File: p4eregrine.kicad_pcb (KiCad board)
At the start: 6 copper layers, 39.5 x 39.5 mm, 357 parts, among them J5 Conn_Coaxial, Q10 NMOS, Q11 NMOS, Q12 NMOS, Q13 NMOS, Q14 NMOS, Q15 NMOS, Q16 NMOS, Q17 NMOS, Q18 NMOS, Q19 NMOS, Q20 NMOS, Q21 NMOS, Q22 NMOS, Q23 NMOS, Q24 NMOS, Q25 NMOS, Q26 NMOS, Q27 NMOS, Q28 NMOS, Q5 NMOS, Q6 NMOS, Q7 NMOS, Q8 NMOS, Q9 NMOS, U10 FPC-1.0FX-15PWCR-H20, U11 VL53L1CXV0FY1, U12 LIS2MDL, U13 LSM6DS3, U14 PMW3901MB-TXQT_C43496881, U15 TPD2EUSB30A, U16 DRV8328ARUYR, U17 TPS62933, U19 DRV8328ARUYR, U2 LPS22HB, U20 STM32G071GBU6, U22 DRV8328ARUYR, U23 STM32G071GBU6, U25 DRV8328ARUYR, U26 STM32G071GBU6, U3 W25Q128JVP, U30 STM32G071GBU6, U4 ESP32-C5HF4, U5 LFD182G45DCHD277, U6 TLV62569DBV, U7 GT-USB-7079C, U8 INA190A2IDCKR, U9 TPS2121RUXR, Y1 Crystal_GND24, Y2 Crystal_GND24

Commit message: Update a couple capacitor footprints
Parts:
- C77, C78: footprint Capacitor_SMD:C_0805_2012Metric -> Capacitor_SMD:C_0603_1608Metric
- R49, R51, R6, R7: footprint Capacitor_SMD:C_0201_0603Metric -> Resistor_SMD:R_0201_0603Metric
- U1: value ~ -> ESP32-P4NRW32X
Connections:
- net /MCU/VDD_PSRAM renamed Net-(U1-VDDO_PSRAM)
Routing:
- net GND: track 237.9 -> 238.8 mm

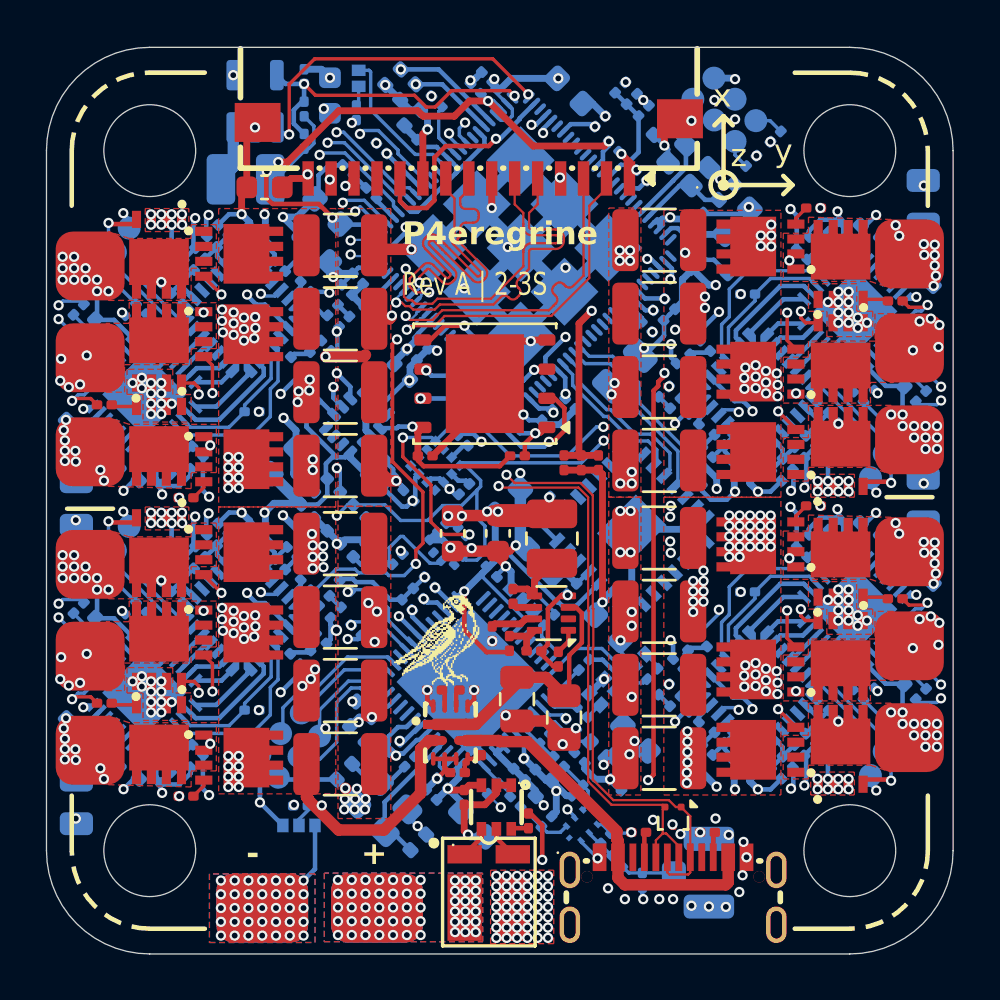
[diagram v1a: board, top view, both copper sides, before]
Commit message: Fix stackup settings in kicad
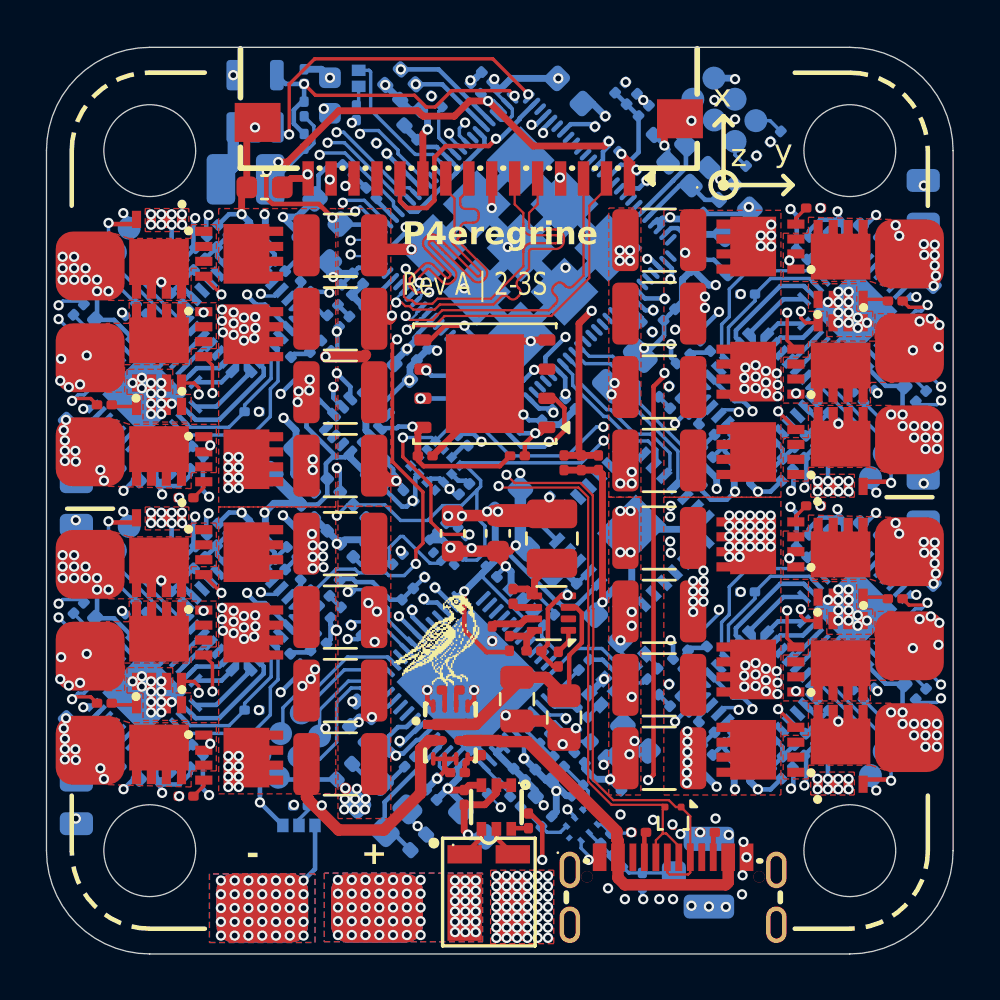
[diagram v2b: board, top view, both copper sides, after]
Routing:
- net GND: track 238.8 -> 238.7 mm, vias 242 -> 243
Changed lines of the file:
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@@
 	(generator_version "10.0")
 	(general
-		(thickness 1.607428)
+		(thickness 1.166)
 		(legacy_teardrops no)
 	)
 	(paper "A4")
 	(layers
-		(0 "F.Cu" signal)
+		(0 "F.Cu" mixed)
 		(4 "In1.Cu" power "F.GND")
 		(6 "In2.Cu" mixed "InF.Cu")
 		(8 "In3.Cu" mixed "InB.Cu")
 		(10 "In4.Cu" power "B.GND")
-		(2 "B.Cu" signal)
+		(2 "B.Cu" mixed)
 		(9 "F.Adhes" user "F.Adhesive")
 		(11 "B.Adhes" user "B.Adhesive")
@@
 		(31 "F.CrtYd" user "F.Courtyard")
 		(29 "B.CrtYd" user "B.Courtyard")
-		(35 "F.Fab" user)
-		(33 "B.Fab" user)
-		(39 "User.1" user)
-		(41 "User.2" user)
-		(43 "User.3" user)
-		(45 "User.4" user)
 	)
 	(setup
@@
 			(layer "dielectric 1"
 				(type "prepreg")
-				(thickness 0.1)
+				(thickness 0.0994)
 				(material "FR4")
 				(epsilon_r 4.1)
@@
 			(layer "dielectric 2"
 				(type "core")
-				(thickness 0.578314)
+				(thickness 0.35)
 				(material "FR4")
 				(epsilon_r 4.6)
@@
 			(layer "dielectric 3"
 				(type "prepreg")
-				(thickness 0.1)
+				(thickness 0.1164)
 				(material "FR4")
 				(epsilon_r 4.1)
@@
 			(layer "dielectric 4"
 				(type "core")
-				(thickness 0.578314)
+				(thickness 0.35)
 				(material "FR4")
 				(epsilon_r 4.6)
@@
 			(layer "dielectric 5"
 				(type "prepreg")
-				(thickness 0.1)
+				(thickness 0.0994)
 				(material "FR4")
 				(epsilon_r 4.1)
@@
 			)
 			(copper_finish "ENIG")
-			(dielectric_constraints no)
+			(dielectric_constraints yes)
 		)
 		(pad_to_mask_clearance 0)
@@
 		(capping no)
 		(filling no)
+		(zone_defaults)
 		(pcbplotparams
 			(layerselection 0x00000000_00000000_55555555_5755f5ff)
@@
 	)
 	(via
-		(at 154.308578 105.428588)
+		(at 153.916729 105.497599)
 		(size 0.45)
 		(drill 0.25)
@@
 	)
 	(via
-		(at 160.482955 106.896387)
+		(at 160.6 107)
 		(size 0.45)
 		(drill 0.25)
@@
 	)
 	(via
+		(at 155.307116 103.523366)
+		(size 0.45)
+		(drill 0.25)
+		(layers "F.Cu" "B.Cu")
+		(remove_unused_layers yes)
+		(keep_end_layers yes)
+		(zone_layer_connections "In1.Cu" "In4.Cu")
+		(net "GND")
+	)
+	(via
 		(at 165.243759 101.971387)
 		(size 0.45)
@@
 	)
 	(segment
+		(start 153.916729 105.497599)
+		(end 153.916729 105.316729)
+		(width 0.15)
+		(layer "B.Cu")
+		(net "GND")
+	)
+	(segment
 		(start 158.75553 101.56816)
 		(end 159.493759 102.306389)
@@
 	)
 	(segment
+		(start 153.590438 104.990438)
+		(end 153.590438 104.661891)
+		(width 0.15)
+		(layer "B.Cu")
+		(net "GND")
+	)
+	(segment
 		(start 155.301278 94.349078)
 		(end 155.301278 95.929463)
@@
 	)
 	(segment
+		(start 153.916729 105.316729)
+		(end 153.590438 104.990438)
+		(width 0.15)
+		(layer "B.Cu")
+		(net "GND")
+	)
+	(segment
 		(start 147.983081 101.105144)
 		(end 148.796254 100.29197)
@@
 	)
 	(segment
-		(start 153.590438 104.710448)
-		(end 154.308578 105.428588)
-		(width 0.15)
-		(layer "B.Cu")
-		(net "GND")
-	)
-	(segment
 		(start 164.822527 77.303431)
 		(end 164.760481 77.241385)
@@
 	)
 	(segment
-		(start 153.590438 104.661891)
-		(end 153.590438 104.710448)
-		(width 0.15)
-		(layer "B.Cu")
-		(net "GND")
-	)
-	(segment
 		(start 159.649339 75.843301)
 		(end 159.869159 76.063122)
@@
 	)
 	(segment
-		(start 156.746253 85.056269)
-		(end 156.746253 101.78151)
+		(start 157.221772 84.399116)
+		(end 156.746253 84.874635)
 		(width 0.2)
 		(layer "F.Cu")
@@
 	)
 	(segment
-		(start 151.383999 103.476387)
-		(end 151.896253 103.988641)
+		(start 156.746253 84.874635)
+		(end 156.746253 101.78151)
 		(width 0.2)
 		(layer "F.Cu")
@@
 	)
 	(segment
-		(start 156.948801 84.853721)
-		(end 156.746253 85.056269)
+		(start 151.383999 103.476387)
+		(end 151.896253 103.988641)
 		(width 0.2)
 		(layer "F.Cu")
@@
 	)
 	(segment
-		(start 157.221772 84.399116)
-		(end 156.948801 84.672087)
-		(width 0.2)
-		(layer "F.Cu")
-		(net "BAT_ISENSE")
-	)
-	(segment
-		(start 156.948801 84.672087)
-		(end 156.948801 84.853721)
-		(width 0.2)
-		(layer "F.Cu")
-		(net "BAT_ISENSE")
-	)
-	(segment
 		(start 157.221772 84.285377)
 		(end 157.221772 84.399116)
@@
 	)
 	(segment
+		(start 146.731115 74.436775)
+		(end 147.297479 74.436776)
+		(width 0.2)
+		(layer "B.Cu")
+		(net "Net-(U1-VDDO_PSRAM)")
+	)
+	(segment
+		(start 149.378576 74.332946)
+		(end 148.141139 75.570383)
+		(width 0.2)
+		(layer "B.Cu")
+		(net "Net-(U1-VDDO_PSRAM)")
+	)
+	(segment
+		(start 146.161239 77.260334)
+		(end 146.45119 77.260334)
+		(width 0.2)
+		(layer "B.Cu")
+		(net "Net-(U1-VDDO_PSRAM)")
+	)
+	(segment
+		(start 145.889658 73.567035)
+		(end 145.833091 73.567035)
+		(width 0.3)
+		(layer "B.Cu")
+		(net "Net-(U1-VDDO_PSRAM)")
+	)
+	(segment
+		(start 146.49777 74.175146)
+		(end 145.889658 73.567035)
+		(width 0.3)
+		(layer "B.Cu")
+		(net "Net-(U1-VDDO_PSRAM)")
+	)
+	(segment
+		(start 148.141139 75.570383)
+		(end 148.141138 75.280435)
+		(width 0.2)
+		(layer "B.Cu")
+		(net "Net-(U1-VDDO_PSRAM)")
+	)
+	(segment
+		(start 148.141138 75.280435)
+		(end 147.879528 75.018823)
+		(width 0.2)
+		(layer "B.Cu")
+		(net "Net-(U1-VDDO_PSRAM)")
+	)
+	(segment
+		(start 149.378576 74.042997)
+		(end 149.378576 74.332946)
+		(width 0.2)
+		(layer "B.Cu")
+		(net "Net-(U1-VDDO_PSRAM)")
+	)
+	(segment
+		(start 146.45119 77.260334)
+		(end 148.141139 75.570383)
+		(width 0.2)
+		(layer "B.Cu")
+		(net "Net-(U1-VDDO_PSRAM)")
+	)
+	(segment
+		(start 147.297479 74.436776)
+		(end 147.879528 75.018823)
+		(width 0.2)
+		(layer "B.Cu")
+		(net "Net-(U1-VDDO_PSRAM)")
+	)
+	(segment
+		(start 145.899629 76.998722)
+		(end 146.161239 77.260334)
+		(width 0.2)
+		(layer "B.Cu")
+		(net "Net-(U1-VDDO_PSRAM)")
+	)
+	(segment
+		(start 149.116964 73.781386)
+		(end 149.378576 74.042997)
+		(width 0.2)
+		(layer "B.Cu")
+		(net "Net-(U1-VDDO_PSRAM)")
+	)
+	(segment
+		(start 146.412918 74.118578)
+		(end 146.731115 74.436775)
+		(width 0.2)
+		(layer "B.Cu")
+		(net "Net-(U1-VDDO_PSRAM)")
+	)
+	(segment
 		(start 167.939739 93.115213)
 		(end 168.268561 92.786391)
@@
 		(net "/Motors/ESC3/SWCLK")
 	)
-	(segment
-		(start 146.731115 74.436775)
-		(end 147.297479 74.436776)
-		(width 0.2)
-		(layer "B.Cu")
-		(net "Net-(U1-VDDO_PSRAM)")
-	)
-	(segment
-		(start 149.378576 74.332946)
-		(end 148.141139 75.570383)
-		(width 0.2)
-		(layer "B.Cu")
-		(net "Net-(U1-VDDO_PSRAM)")
-	)
-	(segment
-		(start 146.161239 77.260334)
-		(end 146.45119 77.260334)
-		(width 0.2)
-		(layer "B.Cu")
-		(net "Net-(U1-VDDO_PSRAM)")
-	)
-	(segment
-		(start 145.889658 73.567035)
-		(end 145.833091 73.567035)
-		(width 0.3)
-		(layer "B.Cu")
-		(net "Net-(U1-VDDO_PSRAM)")
-	)
-	(segment
-		(start 146.49777 74.175146)
-		(end 145.889658 73.567035)
-		(width 0.3)
-		(layer "B.Cu")
-		(net "Net-(U1-VDDO_PSRAM)")
-	)
-	(segment
-		(start 148.141139 75.570383)
-		(end 148.141138 75.280435)
-		(width 0.2)
-		(layer "B.Cu")
-		(net "Net-(U1-VDDO_PSRAM)")
-	)
-	(segment
-		(start 148.141138 75.280435)
-		(end 147.879528 75.018823)
-		(width 0.2)
-		(layer "B.Cu")
-		(net "Net-(U1-VDDO_PSRAM)")
-	)
-	(segment
-		(start 149.378576 74.042997)
-		(end 149.378576 74.332946)
-		(width 0.2)
-		(layer "B.Cu")
-		(net "Net-(U1-VDDO_PSRAM)")
-	)
-	(segment
-		(start 146.45119 77.260334)
-		(end 148.141139 75.570383)
-		(width 0.2)
-		(layer "B.Cu")
-		(net "Net-(U1-VDDO_PSRAM)")
-	)
-	(segment
-		(start 147.297479 74.436776)
-		(end 147.879528 75.018823)
-		(width 0.2)
-		(layer "B.Cu")
-		(net "Net-(U1-VDDO_PSRAM)")
-	)
-	(segment
-		(start 145.899629 76.998722)
-		(end 146.161239 77.260334)
-		(width 0.2)
-		(layer "B.Cu")
-		(net "Net-(U1-VDDO_PSRAM)")
-	)
-	(segment
-		(start 149.116964 73.781386)
-		(end 149.378576 74.042997)
-		(width 0.2)
-		(layer "B.Cu")
-		(net "Net-(U1-VDDO_PSRAM)")
-	)
-	(segment
-		(start 146.412918 74.118578)
-		(end 146.731115 74.436775)
-		(width 0.2)
-		(layer "B.Cu")
-		(net "Net-(U1-VDDO_PSRAM)")
-	)
 	(zone

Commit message: Remove unused layers
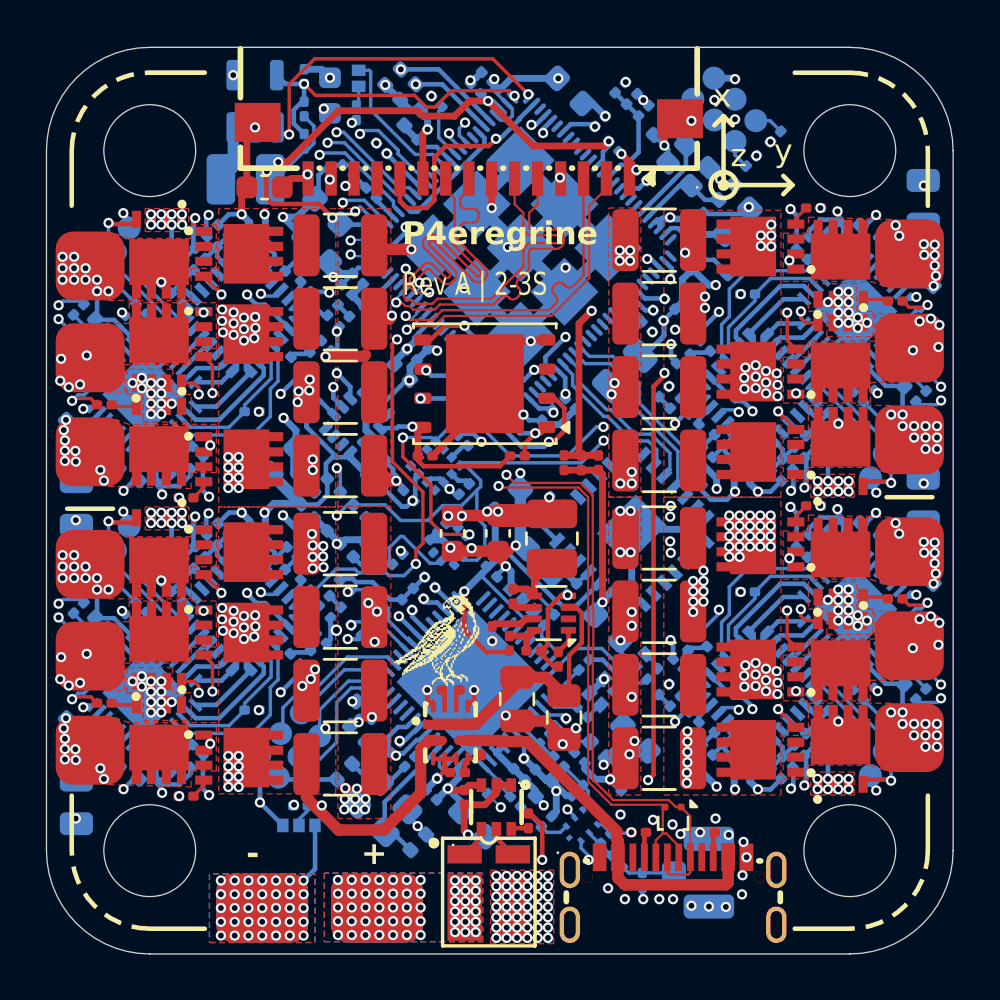
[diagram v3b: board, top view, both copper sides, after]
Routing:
- net +3V3: track 137.9 -> 139.6 mm
